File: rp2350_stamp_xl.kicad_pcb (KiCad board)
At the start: 4 copper layers, 45 x 25 mm, 91 parts, among them J1 Conn_North, J2 Conn_West, J3 Conn_East, J4 Conn_South, J5 Conn_Pi_SWD, J6 Conn_Pi_UART, Q1 BSS84, SW1 SW_RESET, SW2 SW_BOOTSEL, U1 W25Q128JVPIQ, U2 ME4055, U3 AP2112K-3.3, U4 FLASH or PSRAM, U5 RP235x-B, Y1 XYDBPCNANF-12MHZ

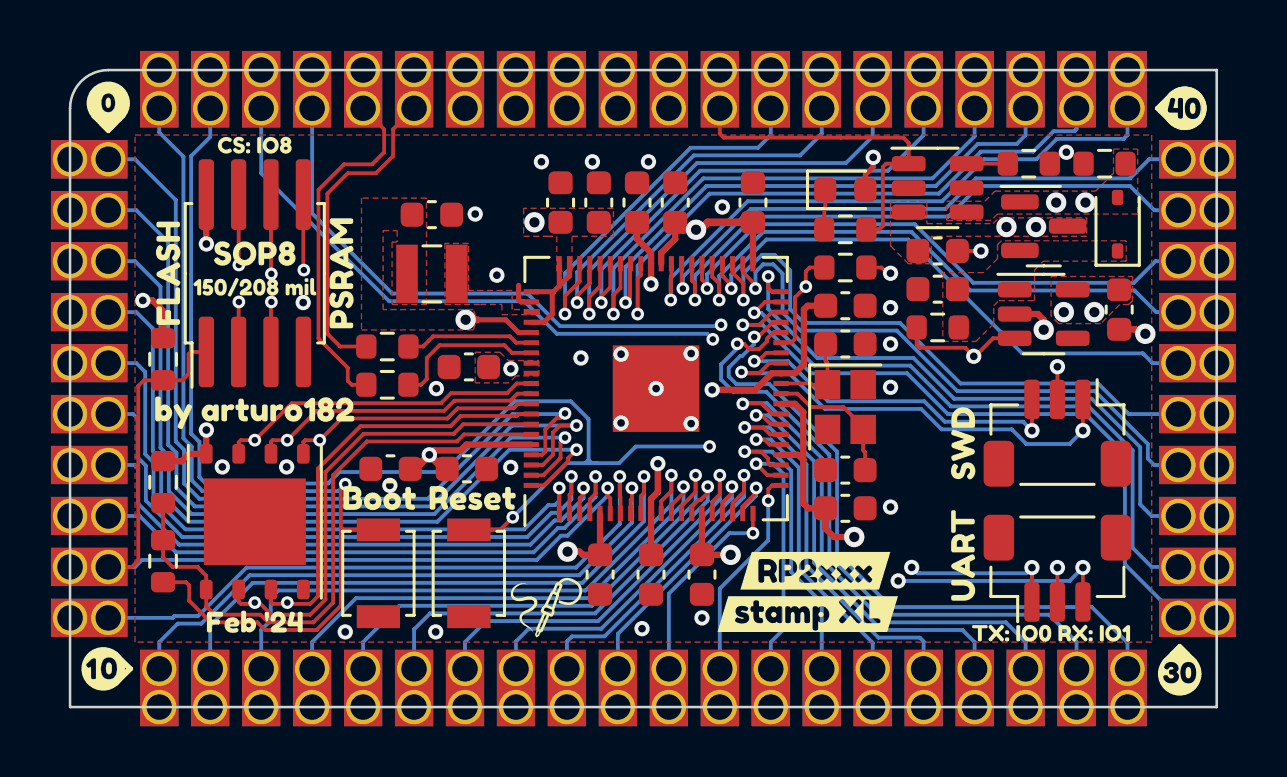
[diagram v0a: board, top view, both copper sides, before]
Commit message: Rev 3
- Rev 2 added logo and QR Code
- Put chip name on the board
- Fixup pin markers to be uniform
- Add battery icon
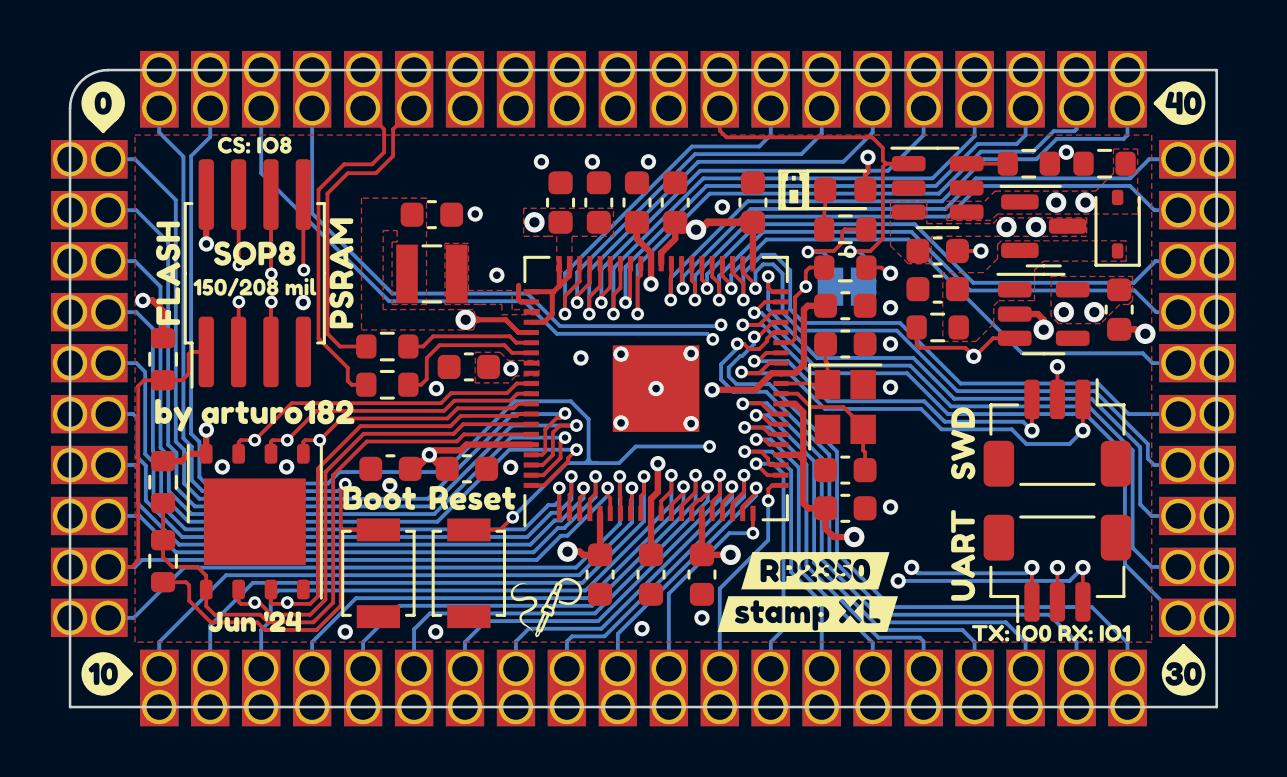
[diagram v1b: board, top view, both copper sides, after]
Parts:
- removed ? (x4): , buzzardLabel
- removed kibuzzard-653BCD7C: G***, kibuzzard-653BCD7C
- removed kibuzzard-653BCEA0 (x2): G***, kibuzzard-653BCEA0
- removed kibuzzard-653BD19C (x2): G***, kibuzzard-653BD19C
- removed kibuzzard-653BD1A6: G***, kibuzzard-653BD1A6
- removed kibuzzard-65C59BA4: G***, kibuzzard-65C59BA4
- removed kibuzzard-65C59BFE: G***, kibuzzard-65C59BFE
- removed the svg2mod at (183.1, 111.0)
- removed the svg2mod at (163.9, 111.0)
- removed the svg2mod at (183.8, 111.0)
- removed the svg2mod at (153.7, 103.2)
- removed the svg2mod at (163.2, 111.0)
- added G***: LOGO, LOGO, B.Cu at (161.7, 104.0)
- added JP1: SJ_STAT_LED, Jumper:SolderJumper-2_P1.3mm_Bridged_RoundedPad1.0x1.5mm, B.Cu at (180.4, 98.2)
- added kibuzzard-6605B0A1: G***, kibuzzard-6605B0A1, B.Cu at (184.9, 98.2)
- added kibuzzard-6605B0D5: G***, kibuzzard-6605B0D5, B.Cu at (187.9, 98.2)
- added kibuzzard-6695ACF2: G***, kibuzzard-6695ACF2, F.Cu at (151.2, 113.5)
- added kibuzzard-6695ACF2: G***, kibuzzard-6695ACF2, B.Cu at (151.2, 113.5)
- added kibuzzard-6695AD18: G***, kibuzzard-6695AD18, F.Cu at (151.2, 91.0)
- added kibuzzard-6695AD18: G***, kibuzzard-6695AD18, B.Cu at (151.2, 91.0)
- added kibuzzard-6695BC9C: G***, kibuzzard-6695BC9C, F.Cu at (179.2, 109.4)
- added kibuzzard-6695BCB6: G***, kibuzzard-6695BCB6, F.Cu at (157.2, 111.4)
- added kibuzzard-6695BF60: G***, kibuzzard-6695BF60, F.Cu at (193.7, 113.5)
- added kibuzzard-6695BF60: G***, kibuzzard-6695BF60, B.Cu at (193.7, 113.5)
- added kibuzzard-6695BFEA: G***, kibuzzard-6695BFEA, F.Cu at (193.7, 91.0)
- added kibuzzard-6695BFEA: G***, kibuzzard-6695BFEA, B.Cu at (193.7, 91.0)
- added kibuzzard-6695C219: G***, kibuzzard-6695C219, B.Cu at (191.2, 101.2)
- added kibuzzard-6695C24F: G***, kibuzzard-6695C24F, B.Cu at (183.4, 111.0)
- added kibuzzard-6695C28C: G***, kibuzzard-6695C28C, B.Cu at (173.4, 111.0)
- added kibuzzard-6695C372: G***, kibuzzard-6695C372, B.Cu at (163.4, 111.1)
- added kibuzzard-6695C3C8: G***, kibuzzard-6695C3C8, B.Cu at (153.7, 103.2)
- added kibuzzard-6695C4C9: G***, kibuzzard-6695C4C9, B.Cu at (177.5, 93.5)
- moved G*** 20.5 mm to (183.4, 105.0)
- moved kibuzzard-6578FE34 0.10 mm to (157.2, 103.3)
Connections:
- R2 pad 1: /BAT_STAT -> Net-(JP1-A)
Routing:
- net Net-(JP1-A): track 0.00 -> 4.97 mm, vias 0 -> 1
- net /BAT_STAT: track 13.5 -> 15.4 mm, vias 0 -> 1
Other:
- board text added: "12mHz"
- board text added: "LED"
- board text added: "Schottky"

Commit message: Rev 3.5
Fixup power stuff according to RPi's recommendations
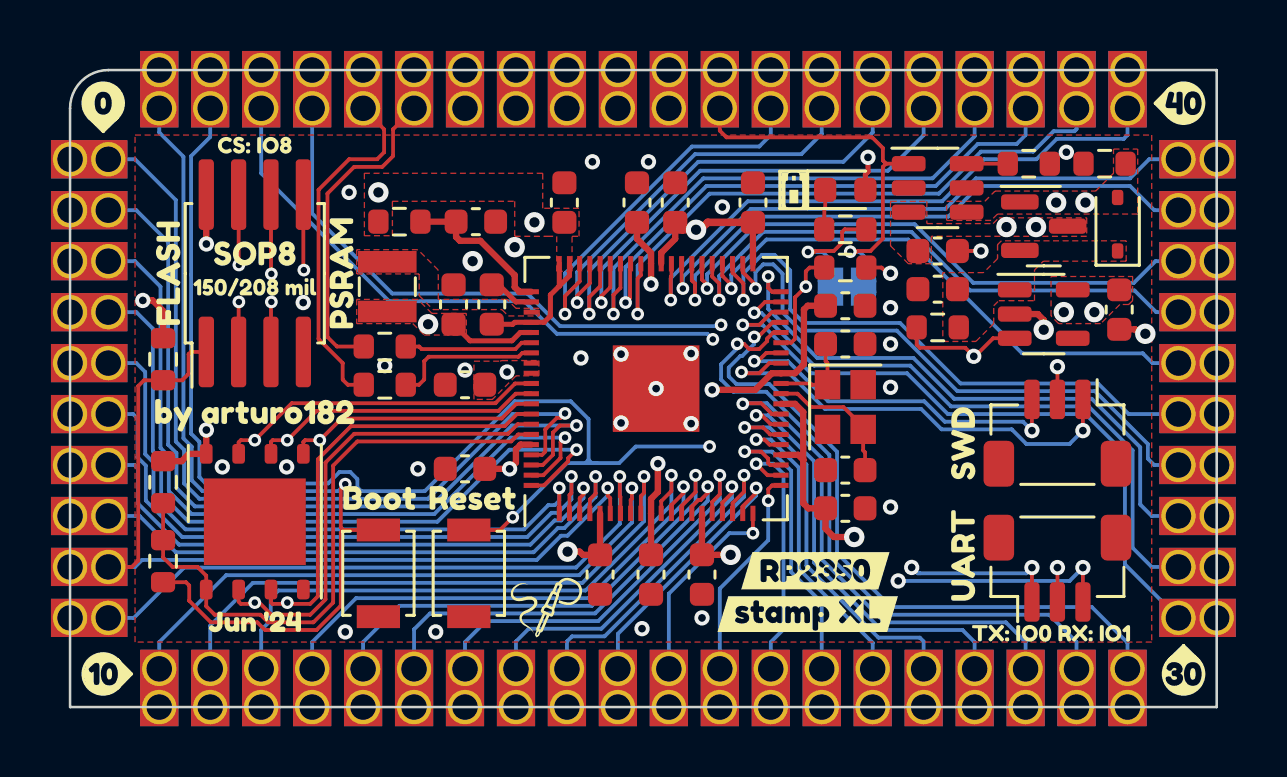
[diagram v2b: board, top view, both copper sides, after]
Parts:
- added R11: 27R, Resistor_SMD:R_0603_1608Metric, F.Cu at (162.9, 95.7)
- C12: value 1uF -> 4.7uF
- C14: value 10uF -> 4.7uF
- L1: value 4.7uH -> 3.3uH
- moved C12 9.71 mm to (165.9, 95.7)
- moved C14 4.83 mm to (166.5, 99.0)
- moved C16 3.63 mm to (165.0, 99.0), turned to 90 degrees
- moved C15 2.92 mm to (165.4, 105.4)
- moved L1 1.82 mm to (162.4, 98.2), turned to 90 degrees
- moved C13 1.35 mm to (169.3, 95.0)
- moved C8 0.72 mm to (165.4, 102.1)
- moved R6 0.10 mm to (162.3, 100.6)
- moved R7 0.10 mm to (162.3, 102.1)
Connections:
- net Net-(U5-VREG_FB) renamed +1.1V
- C12 pad 1: +3V3 -> Net-(U5-VREG_AVDD)
- U5 pad 61: +3V3 -> Net-(U5-VREG_AVDD)
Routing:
- net Net-(U5-VREG_AVDD): track 0.00 -> 6.12 mm
- net +3V3: track 39.8 -> 36.8 mm, vias 13 -> 14
- net +1.1V: track 34.5 -> 36.6 mm
- net /~{RESET}: track 58.3 -> 59.1 mm
- net GND: track 7.36 -> 8.05 mm

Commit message: Fix BOM info, add README and LICENSE
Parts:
- U3: value AP2112K-3.3 -> ME6211
- Y1: value XYDBPCNANF-12MHZ -> CM4012M00012001
